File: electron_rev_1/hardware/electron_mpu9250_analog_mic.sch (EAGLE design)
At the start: 35 parts, among them IC4 MIC_I2S_SPH0645, U1 MPU-9250, U3 OPA322AIDBVT, U4 microSD

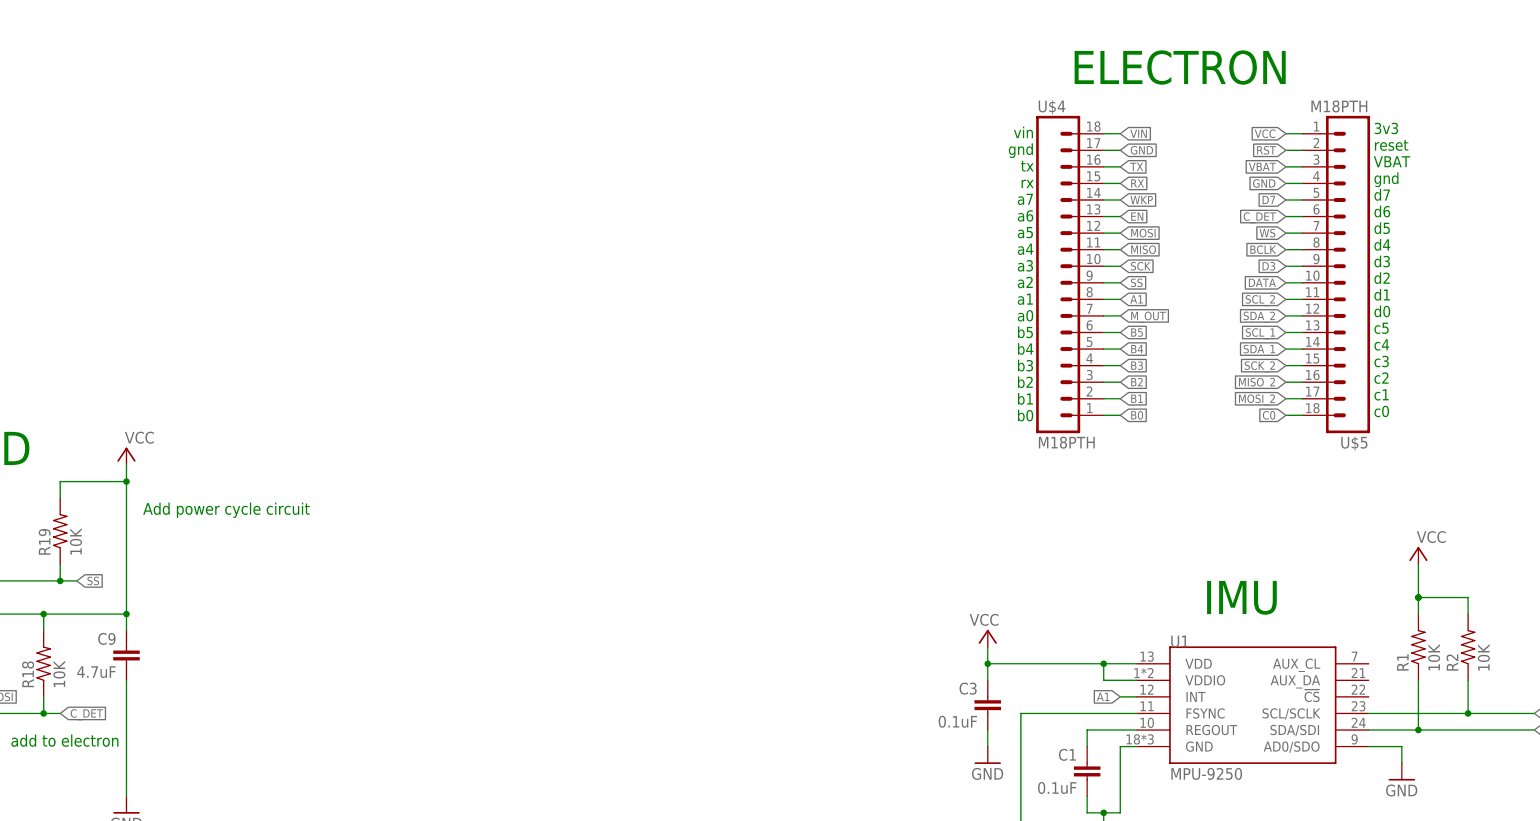
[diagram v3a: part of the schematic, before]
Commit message: reroute w out gas sensor. almost ready to ship
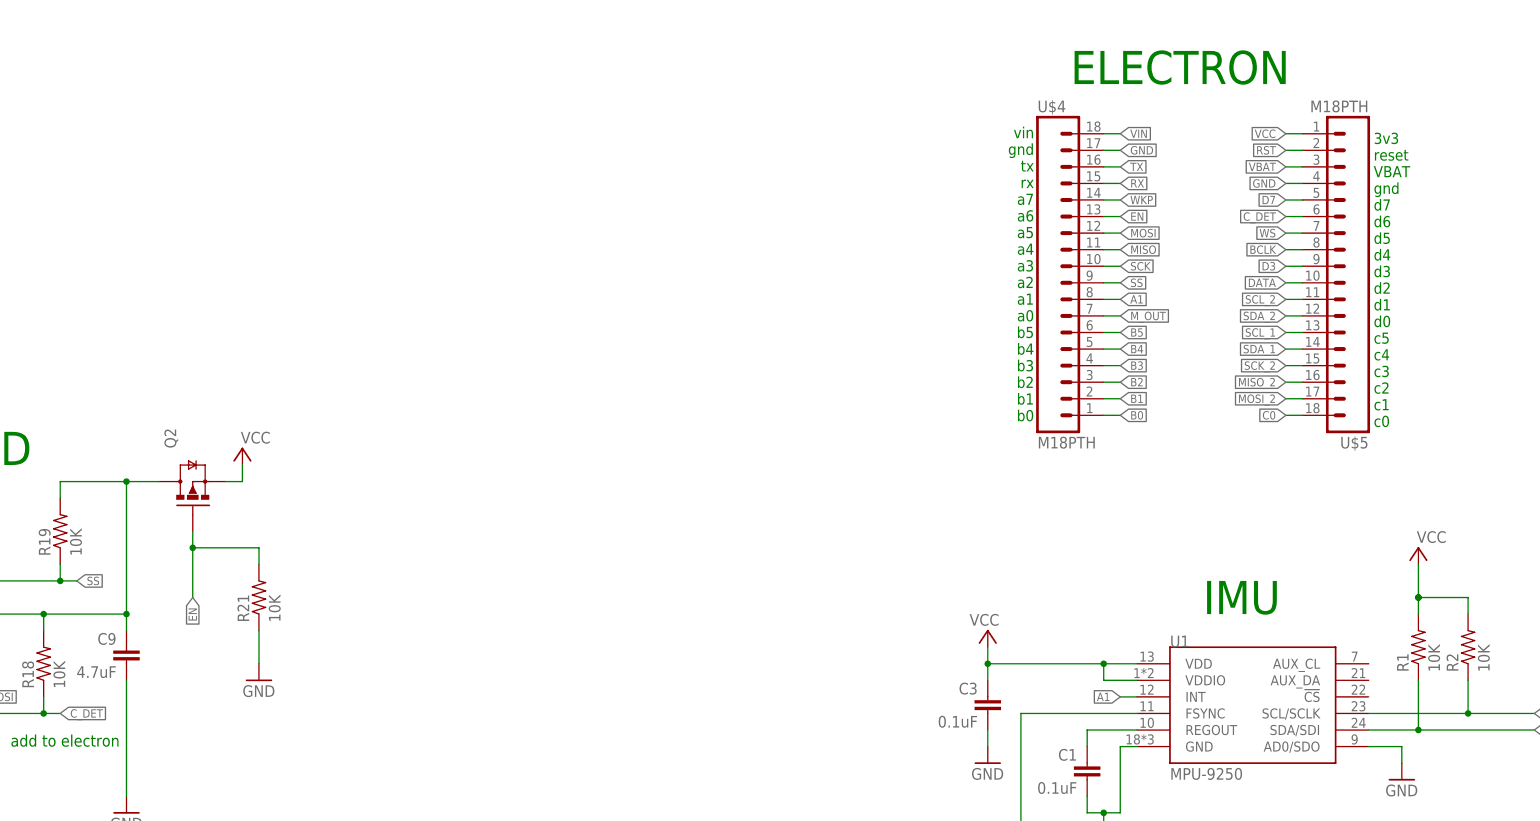
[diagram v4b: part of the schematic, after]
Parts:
- added Q2: NX3008PBK, fets:NX3008PBK
- added R21: 10K, resistor:R-US_R0603
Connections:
- new net N$10: C9.1, Q2.D, R18.2, R19.2, R20.2, U4.VCC
- net EN: now also Q2.G, R21.2
- net GND: now also R21.1
- net VCC: now also Q2.S; no longer C9.1, R18.2, R19.2, R20.2, U4.VCC
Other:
- note removed: "Add power cycle circuit"
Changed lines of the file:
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@@
 <part name="R15" library="resistor" library_urn="urn:adsk.eagle:library:348" deviceset="R-US_" device="R0603" package3d_urn="urn:adsk.eagle:package:26057/1"/>
 <part name="U4" library="SparkFun" deviceset="USD-SOCKET" device="SMD" value="microSD"/>
-<part name="P+6" library="supply1" library_urn="urn:adsk.eagle:library:371" deviceset="VCC" device=""/>
 <part name="FRAME1" library="frames" library_urn="urn:adsk.eagle:library:229" deviceset="A3L-LOC" device=""/>
 <part name="L1" library="logos" deviceset="UCB_CAL" device="100MIL"/>
@@
 <part name="C9" library="SparkFun-Capacitors" deviceset="0.1UF-25V(+80/-20%)(0603)" device="" value="4.7uF"/>
 <part name="GND20" library="supply1" library_urn="urn:adsk.eagle:library:371" deviceset="GND" device=""/>
+<part name="Q2" library="fets" deviceset="NX3008PBK" device=""/>
+<part name="P+7" library="supply1" library_urn="urn:adsk.eagle:library:371" deviceset="VCC" device=""/>
+<part name="R21" library="resistor" library_urn="urn:adsk.eagle:library:348" deviceset="R-US_" device="R0603" package3d_urn="urn:adsk.eagle:package:26057/1" value="10K"/>
+<part name="GND17" library="supply1" library_urn="urn:adsk.eagle:library:371" deviceset="GND" device=""/>
 </parts>
 <sheets>
@@
 <text x="119.38" y="101.6" size="5.08" layer="91">ELECTRON</text>
 <text x="205.74" y="104.14" size="5.08" layer="91">DEBUG</text>
-<text x="-22.86" y="35.56" size="1.778" layer="91">Add power cycle circuit</text>
 <text x="-43.18" y="0" size="1.778" layer="91">add to electron</text>
-<text x="165.862" y="50.546" size="1.7018" layer="91">3v3
+<text x="165.862" y="49.022" size="1.7018" layer="91">3v3
 reset
 VBAT
@@
 <attribute name="VALUE" x="-90.424" y="-7.874" size="1.778" layer="96"/>
 </instance>
-<instance part="P+6" gate="VCC" x="-25.4" y="45.72" smashed="yes">
-<attribute name="VALUE" x="-25.654" y="46.482" size="1.778" layer="96"/>
-</instance>
 <instance part="FRAME1" gate="G$1" x="-101.6" y="-35.56"/>
 <instance part="L1" gate="G$1" x="269.24" y="0"/>
@@
 <instance part="C9" gate="G$1" x="-25.4" y="12.7" rot="MR0"/>
 <instance part="GND20" gate="1" x="-25.4" y="-10.16"/>
+<instance part="Q2" gate="G$1" x="-15.24" y="40.64" smashed="yes" rot="R90">
+<attribute name="NAME" x="-17.78" y="45.72" size="1.778" layer="95" rot="R90"/>
+</instance>
+<instance part="P+7" gate="VCC" x="-7.62" y="45.72" smashed="yes">
+<attribute name="VALUE" x="-7.874" y="46.482" size="1.778" layer="96"/>
+</instance>
+<instance part="R21" gate="G$1" x="-5.08" y="22.86" rot="R90"/>
+<instance part="GND17" gate="1" x="-5.08" y="10.16"/>
 </instances>
 <busses>
@@
 <wire x1="-25.4" y1="10.16" x2="-25.4" y2="-7.62" width="0.1524" layer="91"/>
 </segment>
+<segment>
+<pinref part="R21" gate="G$1" pin="1"/>
+<pinref part="GND17" gate="1" pin="GND"/>
+<wire x1="-5.08" y1="12.7" x2="-5.08" y2="17.78" width="0.1524" layer="91"/>
+</segment>
 </net>
 <net name="TX" class="0">
@@
 </segment>
 <segment>
-<wire x1="-73.66" y1="20.32" x2="-50.8" y2="20.32" width="0.1524" layer="91"/>
-<pinref part="U4" gate="G$1" pin="VCC"/>
-<pinref part="P+6" gate="VCC" pin="VCC"/>
-<wire x1="-50.8" y1="20.32" x2="-38.1" y2="20.32" width="0.1524" layer="91"/>
-<wire x1="-38.1" y1="20.32" x2="-25.4" y2="20.32" width="0.1524" layer="91"/>
-<wire x1="-25.4" y1="20.32" x2="-25.4" y2="40.64" width="0.1524" layer="91"/>
-<pinref part="R18" gate="G$1" pin="2"/>
-<wire x1="-25.4" y1="40.64" x2="-25.4" y2="43.18" width="0.1524" layer="91"/>
-<wire x1="-38.1" y1="17.78" x2="-38.1" y2="20.32" width="0.1524" layer="91"/>
-<junction x="-38.1" y="20.32"/>
-<pinref part="R20" gate="G$1" pin="2"/>
-<wire x1="-50.8" y1="17.78" x2="-50.8" y2="20.32" width="0.1524" layer="91"/>
-<junction x="-50.8" y="20.32"/>
-<pinref part="R19" gate="G$1" pin="2"/>
-<wire x1="-35.56" y1="38.1" x2="-35.56" y2="40.64" width="0.1524" layer="91"/>
-<wire x1="-35.56" y1="40.64" x2="-25.4" y2="40.64" width="0.1524" layer="91"/>
-<junction x="-25.4" y="40.64"/>
-<pinref part="C9" gate="G$1" pin="1"/>
-<wire x1="-25.4" y1="17.78" x2="-25.4" y2="20.32" width="0.1524" layer="91"/>
-<junction x="-25.4" y="20.32"/>
+<pinref part="Q2" gate="G$1" pin="S"/>
+<pinref part="P+7" gate="VCC" pin="VCC"/>
+<wire x1="-10.16" y1="40.64" x2="-7.62" y2="40.64" width="0.1524" layer="91"/>
+<wire x1="-7.62" y1="40.64" x2="-7.62" y2="43.18" width="0.1524" layer="91"/>
 </segment>
 </net>
@@
 <label x="127" y="81.28" size="1.27" layer="95" xref="yes"/>
 </segment>
+<segment>
+<pinref part="Q2" gate="G$1" pin="G"/>
+<wire x1="-15.24" y1="33.02" x2="-15.24" y2="30.48" width="0.1524" layer="91"/>
+<label x="-15.24" y="22.86" size="1.27" layer="95" rot="R270" xref="yes"/>
+<pinref part="R21" gate="G$1" pin="2"/>
+<wire x1="-15.24" y1="30.48" x2="-15.24" y2="22.86" width="0.1524" layer="91"/>
+<wire x1="-15.24" y1="30.48" x2="-5.08" y2="30.48" width="0.1524" layer="91"/>
+<wire x1="-5.08" y1="30.48" x2="-5.08" y2="27.94" width="0.1524" layer="91"/>
+<junction x="-15.24" y="30.48"/>
+</segment>
+</net>
+<net name="N$10" class="0">
+<segment>
+<wire x1="-73.66" y1="20.32" x2="-50.8" y2="20.32" width="0.1524" layer="91"/>
+<pinref part="U4" gate="G$1" pin="VCC"/>
+<wire x1="-50.8" y1="20.32" x2="-38.1" y2="20.32" width="0.1524" layer="91"/>
+<wire x1="-38.1" y1="20.32" x2="-25.4" y2="20.32" width="0.1524" layer="91"/>
+<wire x1="-25.4" y1="20.32" x2="-25.4" y2="40.64" width="0.1524" layer="91"/>
+<pinref part="R18" gate="G$1" pin="2"/>
+<wire x1="-38.1" y1="17.78" x2="-38.1" y2="20.32" width="0.1524" layer="91"/>
+<junction x="-38.1" y="20.32"/>
+<pinref part="R20" gate="G$1" pin="2"/>
+<wire x1="-50.8" y1="17.78" x2="-50.8" y2="20.32" width="0.1524" layer="91"/>
+<junction x="-50.8" y="20.32"/>
+<pinref part="R19" gate="G$1" pin="2"/>
+<wire x1="-35.56" y1="38.1" x2="-35.56" y2="40.64" width="0.1524" layer="91"/>
+<wire x1="-35.56" y1="40.64" x2="-25.4" y2="40.64" width="0.1524" layer="91"/>
+<pinref part="C9" gate="G$1" pin="1"/>
+<wire x1="-25.4" y1="17.78" x2="-25.4" y2="20.32" width="0.1524" layer="91"/>
+<junction x="-25.4" y="20.32"/>
+<pinref part="Q2" gate="G$1" pin="D"/>
+<wire x1="-25.4" y1="40.64" x2="-20.32" y2="40.64" width="0.1524" layer="91"/>
+<junction x="-25.4" y="40.64"/>
+</segment>
 </net>
 </nets>
 </sheet>
 </sheets>
-<errors>
-</errors>
 </schematic>
 </drawing>
